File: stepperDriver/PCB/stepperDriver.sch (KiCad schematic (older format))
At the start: 9 parts, among them J1 grove, M1 Stepper_Motor_bipolar, U1 EL814, U2 ATtiny45-20PU

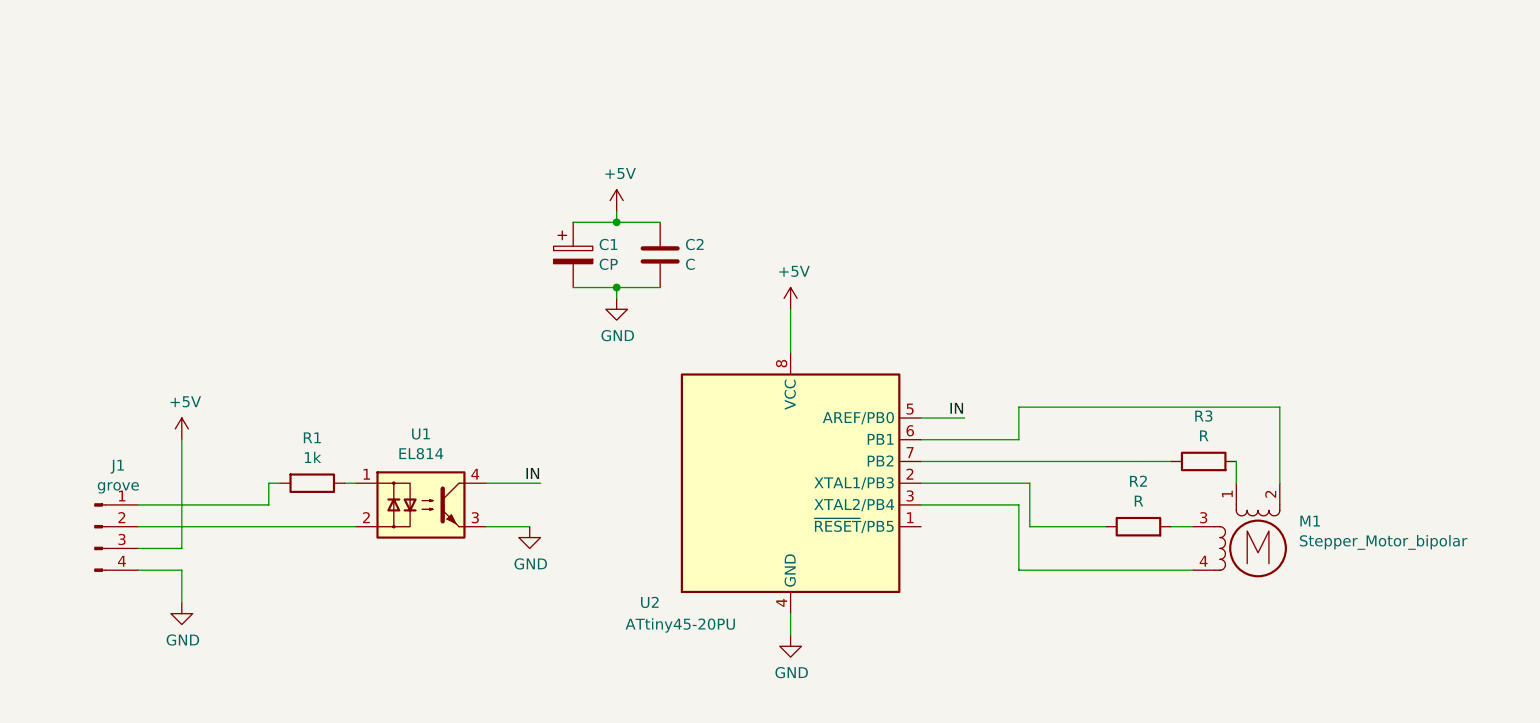
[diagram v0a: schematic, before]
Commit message: changed schematic and made new PCB. I removed the DCC interface and rectifier
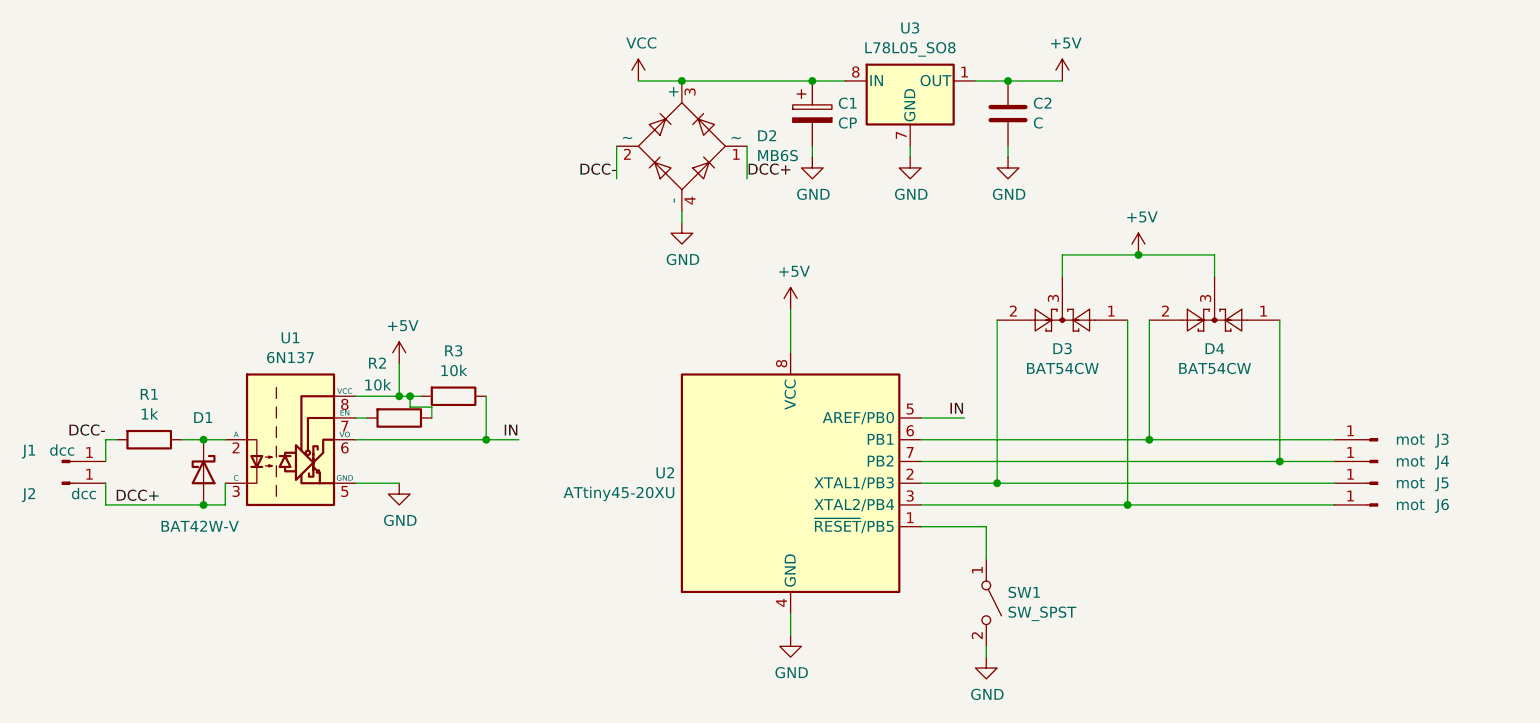
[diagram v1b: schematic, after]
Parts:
- removed J1: grove, Connector:NS-Tech_Grove_1x04_P2mm_Vertical, symbol Connector:Conn_01x04_Male
- removed M1: Stepper_Motor_bipolar, Connector_PinHeader_2.54mm:PinHeader_1x04_P2.54mm_Vertical, symbol Motor:Stepper_Motor_bipolar
- removed U1: EL814, Package_DIP:DIP-4_W7.62mm, symbol Isolator:EL814
- removed U2: ATtiny45-20PU, Package_DIP:DIP-8_W7.62mm, symbol MCU_Microchip_ATtiny:ATtiny45-20PU
- added D1: BAT42W-V, Diode_SMD:D_SOD-123, symbol Diode:BAT42W-V
- added D2: MB6S, Package_TO_SOT_SMD:TO-269AA, symbol Diode_Bridge:MB6S
- added D3, D4: BAT54CW, Package_TO_SOT_SMD:SOT-323_SC-70, symbol Diode:BAT54CW
- added J1, J2: dcc, Connector_Wire:SolderWirePad_1x01_SMD_1x2mm, symbol Connector:Conn_01x01_Male
- added J3, J4, J5, J6: mot, Connector_Wire:SolderWirePad_1x01_SMD_1x2mm, symbol Connector:Conn_01x01_Male
- added SW1: SW_SPST, Button_Switch_SMD:SW_Push_1P1T_NO_CK_KMR2, symbol Switch:SW_SPST
- added U1: 6N137, Package_SO:SOIC-8_3.9x4.9mm_P1.27mm, symbol Isolator:6N137
- added U2: ATtiny45-20XU, Package_SO:TSSOP-8_4.4x3mm_P0.65mm, symbol MCU_Microchip_ATtiny:ATtiny45-20XU
- added U3: L78L05_SO8, Package_SO:SOIC-8_3.9x4.9mm_P1.27mm, symbol Regulator_Linear:L78L05_SO8
- C1: footprint Capacitor_THT:CP_Radial_D4.0mm_P2.00mm -> Capacitor_SMD:CP_Elec_3x5.3
- C2: footprint Capacitor_THT:C_Disc_D3.0mm_W1.6mm_P2.50mm -> Capacitor_SMD:C_0805_2012Metric_Pad1.18x1.45mm_HandSolder
- R1: footprint Resistor_THT:R_Axial_DIN0204_L3.6mm_D1.6mm_P7.62mm_Horizontal -> Resistor_SMD:R_0805_2012Metric_Pad1.20x1.40mm_HandSolder
- R2, R3: value R -> 10k; footprint Resistor_THT:R_Axial_DIN0204_L3.6mm_D1.6mm_P7.62mm_Horizontal -> Resistor_SMD:R_0805_2012Metric_Pad1.20x1.40mm_HandSolder
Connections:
- net +5V: now also R2.1, R3.2, D3.3, D4.3, U1.8 (VCC), U2.8 (VCC), U3.1 (OUT); no longer C1.1
- net GND: now also D2.4 (-), SW1.2 (B), U1.5 (GND), U2.4 (GND), U3.2 (GND), U3.3 (GND), U3.6 (GND), U3.7 (GND)
- net IN: now also R3.1, U1.6 (VO), U2.5 (AREF/PB0)
- net at R2.2: now also U1.7 (EN)
- net at R1.1: now also D1.1 (K), U1.2 (A)
- net DCC-: now reaches R1.2
- net DCC-: now also D2.2 (~~), J1.1 (Pin_1)
- new net: D3.1, J6.1 (Pin_1), U2.3 (XTAL2/PB4)
- new net: D3.2, J5.1 (Pin_1), U2.2 (XTAL1/PB3)
- new net: D4.1, J4.1 (Pin_1), U2.7 (PB2)
- new net: D4.2, J3.1 (Pin_1), U2.6 (PB1)
- new net: SW1.1 (A), U2.1 (~RESET~/PB5)
- new net DCC+: D1.2 (A), D2.1 (~~), J2.1 (Pin_1), U1.3 (C)
- new net VCC: C1.1, D2.3 (+), U3.8 (IN)
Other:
- moved on the sheet: R1
